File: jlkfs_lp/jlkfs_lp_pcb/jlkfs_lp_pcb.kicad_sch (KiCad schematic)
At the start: 40 parts, among them J0 USB_C_Receptacle_PowerOnly_6P, SW0 SWITCH, SW1 SWITCH, SW10 SWITCH, SW11 SWITCH, SW12 SWITCH, SW13 SWITCH, SW14 SWITCH, SW15 SWITCH, SW16 SWITCH, SW17 SWITCH, SW18 SWITCH, SW19 SWITCH, SW2 SWITCH, SW20 SWITCH, SW21 SWITCH, SW22 SWITCH, SW23 SWITCH, SW24 SWITCH, SW25 SWITCH, SW26 SWITCH, SW27 SWITCH, SW28 SWITCH, SW3 SWITCH, SW4 SWITCH, SW5 SWITCH, SW6 SWITCH, SW7 SWITCH, SW8 SWITCH, SW9 SWITCH, U0 RP2040

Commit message: Updates to jlkfs_lp.
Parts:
- removed H4, H5: MountingHole, MountingHole:MountingHole_3.5mm, symbol Mechanical:MountingHole
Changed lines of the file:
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@@
     (pin "11")
     (instances
-      (project "jlkfs_lower"
+      (project "jlkfs_lp_pcb"
         (path "/97127b28-60f4-45ff-835e-dccfbc833331"
           (reference "U0") (unit 1)
@@
     (pin "2")
     (instances
-      (project "jlkfs_lower"
+      (project "jlkfs_lp_pcb"
         (path "/97127b28-60f4-45ff-835e-dccfbc833331"
           (reference "SW13") (unit 1)
@@
     )
   )
-  (symbol (lib_id "Mechanical:MountingHole") (at 134.62 250.19 0) (unit 1)
-    (in_bom yes) (on_board yes) (dnp no) (fields_autoplaced)
-    (property "Reference" "H4" (at 137.16 248.92 0)
-      (effects (font (size 1.27 1.27)) (justify left))
-    )
-    (property "Value" "MountingHole" (at 137.16 251.46 0)
-      (effects (font (size 1.27 1.27)) (justify left))
-    )
-    (property "Footprint" "MountingHole:MountingHole_3.5mm" (at 134.62 250.19 0)
-      (effects (font (size 1.27 1.27)) hide)
-    )
-    (property "Datasheet" "~" (at 134.62 250.19 0)
-      (effects (font (size 1.27 1.27)) hide)
-    )
-    (instances
-      (project "jlkfs_lower"
-        (path "/97127b28-60f4-45ff-835e-dccfbc833331"
-          (reference "H4") (unit 1)
-        )
-      )
-    )
-  )
   (symbol (lib_id "symbols:SWITCH_WITH_DIODE") (at 198.12 77.47 0) (unit 1)
     (in_bom yes) (on_board yes) (dnp no) (fields_autoplaced)
@@
     (pin "2")
     (instances
-      (project "jlkfs_lower"
+      (project "jlkfs_lp_pcb"
         (path "/97127b28-60f4-45ff-835e-dccfbc833331"
           (reference "SW11") (unit 1)
@@
     (pin "2")
     (instances
-      (project "jlkfs_lower"
+      (project "jlkfs_lp_pcb"
         (path "/97127b28-60f4-45ff-835e-dccfbc833331"
           (reference "SW23") (unit 1)
@@
     (pin "2")
     (instances
-      (project "jlkfs_lower"
+      (project "jlkfs_lp_pcb"
         (path "/97127b28-60f4-45ff-835e-dccfbc833331"
           (reference "SW14") (unit 1)
@@
     (pin "2")
     (instances
-      (project "jlkfs_lower"
+      (project "jlkfs_lp_pcb"
         (path "/97127b28-60f4-45ff-835e-dccfbc833331"
           (reference "SW20") (unit 1)
@@
     (pin "2")
     (instances
-      (project "jlkfs_lower"
+      (project "jlkfs_lp_pcb"
         (path "/97127b28-60f4-45ff-835e-dccfbc833331"
           (reference "SW10") (unit 1)
@@
     (pin "2")
     (instances
-      (project "jlkfs_lower"
+      (project "jlkfs_lp_pcb"
         (path "/97127b28-60f4-45ff-835e-dccfbc833331"
           (reference "SW27") (unit 1)
@@
     (pin "2")
     (instances
-      (project "jlkfs_lower"
+      (project "jlkfs_lp_pcb"
         (path "/97127b28-60f4-45ff-835e-dccfbc833331"
           (reference "SW15") (unit 1)
@@
     (pin "2")
     (instances
-      (project "jlkfs_lower"
+      (project "jlkfs_lp_pcb"
         (path "/97127b28-60f4-45ff-835e-dccfbc833331"
           (reference "SW1") (unit 1)
@@
     (pin "2")
     (instances
-      (project "jlkfs_lower"
+      (project "jlkfs_lp_pcb"
         (path "/97127b28-60f4-45ff-835e-dccfbc833331"
           (reference "SW18") (unit 1)
@@
     (pin "2")
     (instances
-      (project "jlkfs_lower"
+      (project "jlkfs_lp_pcb"
         (path "/97127b28-60f4-45ff-835e-dccfbc833331"
           (reference "SW8") (unit 1)
@@
     (pin "2")
     (instances
-      (project "jlkfs_lower"
+      (project "jlkfs_lp_pcb"
         (path "/97127b28-60f4-45ff-835e-dccfbc833331"
           (reference "SW4") (unit 1)
@@
     (pin "2")
     (instances
-      (project "jlkfs_lower"
+      (project "jlkfs_lp_pcb"
         (path "/97127b28-60f4-45ff-835e-dccfbc833331"
           (reference "SW16") (unit 1)
@@
     (pin "2")
     (instances
-      (project "jlkfs_lower"
+      (project "jlkfs_lp_pcb"
         (path "/97127b28-60f4-45ff-835e-dccfbc833331"
           (reference "SW22") (unit 1)
@@
     (pin "2")
     (instances
-      (project "jlkfs_lower"
+      (project "jlkfs_lp_pcb"
         (path "/97127b28-60f4-45ff-835e-dccfbc833331"
           (reference "SW2") (unit 1)
@@
     (pin "2")
     (instances
-      (project "jlkfs_lower"
+      (project "jlkfs_lp_pcb"
         (path "/97127b28-60f4-45ff-835e-dccfbc833331"
           (reference "SW0") (unit 1)
@@
     )
     (instances
-      (project "jlkfs_lower"
+      (project "jlkfs_lp_pcb"
         (path "/97127b28-60f4-45ff-835e-dccfbc833331"
           (reference "H0") (unit 1)
@@
     (pin "2")
     (instances
-      (project "jlkfs_lower"
+      (project "jlkfs_lp_pcb"
         (path "/97127b28-60f4-45ff-835e-dccfbc833331"
           (reference "SW12") (unit 1)
@@
     )
     (instances
-      (project "jlkfs_lower"
+      (project "jlkfs_lp_pcb"
         (path "/97127b28-60f4-45ff-835e-dccfbc833331"
           (reference "H3") (unit 1)
@@
     (pin "1")
     (instances
-      (project "jlkfs_lower"
+      (project "jlkfs_lp_pcb"
         (path "/97127b28-60f4-45ff-835e-dccfbc833331"
           (reference "#PWR01") (unit 1)
@@
     (pin "2")
     (instances
-      (project "jlkfs_lower"
+      (project "jlkfs_lp_pcb"
         (path "/97127b28-60f4-45ff-835e-dccfbc833331"
           (reference "SW5") (unit 1)
@@
     (pin "2")
     (instances
-      (project "jlkfs_lower"
+      (project "jlkfs_lp_pcb"
         (path "/97127b28-60f4-45ff-835e-dccfbc833331"
           (reference "R1") (unit 1)
@@
     (pin "1")
     (instances
-      (project "jlkfs_lower"
+      (project "jlkfs_lp_pcb"
         (path "/97127b28-60f4-45ff-835e-dccfbc833331"
           (reference "#PWR02") (unit 1)
@@
     (pin "2")
     (instances
-      (project "jlkfs_lower"
+      (project "jlkfs_lp_pcb"
         (path "/97127b28-60f4-45ff-835e-dccfbc833331"
           (reference "SW7") (unit 1)
@@
     (pin "2")
     (instances
-      (project "jlkfs_lower"
+      (project "jlkfs_lp_pcb"
         (path "/97127b28-60f4-45ff-835e-dccfbc833331"
           (reference "SW9") (unit 1)
@@
     (pin "2")
     (instances
-      (project "jlkfs_lower"
+      (project "jlkfs_lp_pcb"
         (path "/97127b28-60f4-45ff-835e-dccfbc833331"
           (reference "SW3") (unit 1)
@@
     (pin "2")
     (instances
-      (project "jlkfs_lower"
+      (project "jlkfs_lp_pcb"
         (path "/97127b28-60f4-45ff-835e-dccfbc833331"
           (reference "SW26") (unit 1)
@@
     )
     (instances
-      (project "jlkfs_lower"
+      (project "jlkfs_lp_pcb"
         (path "/97127b28-60f4-45ff-835e-dccfbc833331"
           (reference "H2") (unit 1)
@@
     (pin "1")
     (instances
-      (project "jlkfs_lower"
+      (project "jlkfs_lp_pcb"
         (path "/97127b28-60f4-45ff-835e-dccfbc833331"
           (reference "#PWR00") (unit 1)
@@
     (pin "2")
     (instances
-      (project "jlkfs_lower"
+      (project "jlkfs_lp_pcb"
         (path "/97127b28-60f4-45ff-835e-dccfbc833331"
           (reference "SW24") (unit 1)
@@
     (pin "2")
     (instances
-      (project "jlkfs_lower"
+      (project "jlkfs_lp_pcb"
         (path "/97127b28-60f4-45ff-835e-dccfbc833331"
           (reference "SW28") (unit 1)
@@
     (pin "2")
     (instances
-      (project "jlkfs_lower"
+      (project "jlkfs_lp_pcb"
         (path "/97127b28-60f4-45ff-835e-dccfbc833331"
           (reference "R0") (unit 1)
@@
     (pin "2")
     (instances
-      (project "jlkfs_lower"
+      (project "jlkfs_lp_pcb"
         (path "/97127b28-60f4-45ff-835e-dccfbc833331"
           (reference "SW21") (unit 1)
@@
     )
     (instances
-      (project "jlkfs_lower"
+      (project "jlkfs_lp_pcb"
         (path "/97127b28-60f4-45ff-835e-dccfbc833331"
           (reference "H1") (unit 1)
@@
     (pin "2")
     (instances
-      (project "jlkfs_lower"
+      (project "jlkfs_lp_pcb"
         (path "/97127b28-60f4-45ff-835e-dccfbc833331"
           (reference "SW6") (unit 1)
@@
     (pin "2")
     (instances
-      (project "jlkfs_lower"
+      (project "jlkfs_lp_pcb"
         (path "/97127b28-60f4-45ff-835e-dccfbc833331"
           (reference "SW25") (unit 1)
@@
     (pin "A12")
     (instances
-      (project "jlkfs_lower"
+      (project "jlkfs_lp_pcb"
         (path "/97127b28-60f4-45ff-835e-dccfbc833331"
           (reference "J0") (unit 1)
@@
     (pin "2")
     (instances
-      (project "jlkfs_lower"
+      (project "jlkfs_lp_pcb"
         (path "/97127b28-60f4-45ff-835e-dccfbc833331"
           (reference "SW17") (unit 1)
@@
     (pin "2")
     (instances
-      (project "jlkfs_lower"
+      (project "jlkfs_lp_pcb"
         (path "/97127b28-60f4-45ff-835e-dccfbc833331"
           (reference "RST0") (unit 1)
@@
     )
   )
-  (symbol (lib_id "Mechanical:MountingHole") (at 138.43 250.19 0) (unit 1)
-    (in_bom yes) (on_board yes) (dnp no) (fields_autoplaced)
-    (property "Reference" "H5" (at 140.97 248.92 0)
-      (effects (font (size 1.27 1.27)) (justify left))
-    )
-    (property "Value" "MountingHole" (at 140.97 251.46 0)
-      (effects (font (size 1.27 1.27)) (justify left))
-    )
-    (property "Footprint" "MountingHole:MountingHole_3.5mm" (at 138.43 250.19 0)
-      (effects (font (size 1.27 1.27)) hide)
-    )
-    (property "Datasheet" "~" (at 138.43 250.19 0)
-      (effects (font (size 1.27 1.27)) hide)
-    )
-    (instances
-      (project "jlkfs_lower"
-        (path "/97127b28-60f4-45ff-835e-dccfbc833331"
-          (reference "H5") (unit 1)
-        )
-      )
-    )
-  )
   (symbol (lib_id "symbols:SWITCH_WITH_DIODE") (at 30.48 105.41 0) (unit 1)
     (in_bom yes) (on_board yes) (dnp no) (fields_autoplaced)
@@
     (pin "2")
     (instances
-      (project "jlkfs_lower"
+      (project "jlkfs_lp_pcb"
         (path "/97127b28-60f4-45ff-835e-dccfbc833331"
           (reference "SW19") (unit 1)

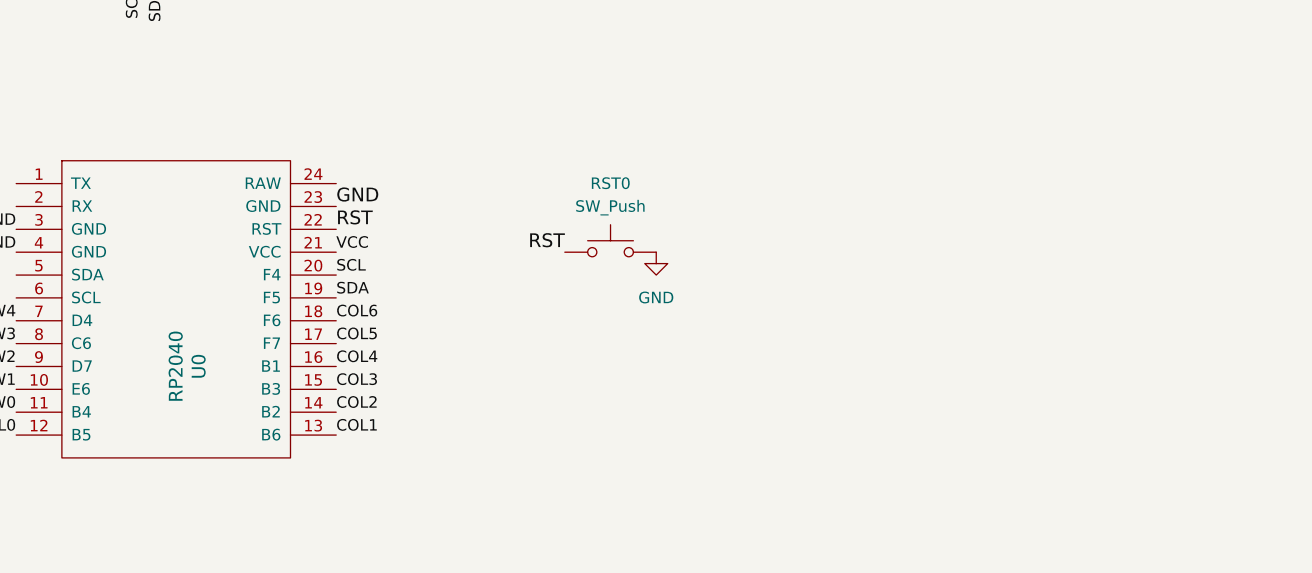
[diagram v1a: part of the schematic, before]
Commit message: Added a battery path for nice!nano to jlkfs.
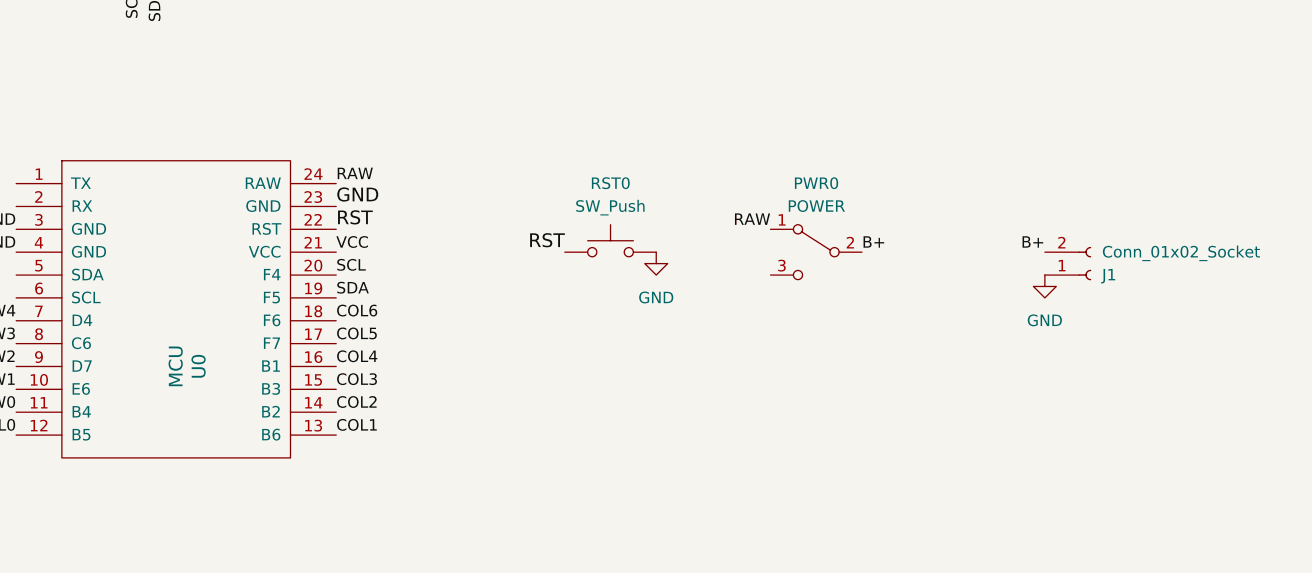
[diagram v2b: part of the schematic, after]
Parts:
- added J1: Conn_01x02_Socket, Connector_PinHeader_2.54mm:PinHeader_1x02_P2.54mm_Vertical, symbol Connector:Conn_01x02_Socket
- added PWR0: POWER, footprints:power_switch_1, symbol Switch:SW_SPDT
- U0: value RP2040 -> MCU
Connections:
- net GND: now also J1.1 (Pin_1)
- net RAW: now reaches U0.24 (RAW)
- net RAW: now also PWR0.1 (A)
- new net B+: J1.2 (Pin_2), PWR0.2 (B)
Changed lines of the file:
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@@
+    (effects (font (size 1.27 1.27)) (justify right bottom))
+  )
+  (label "B+" (at 215.9 198.12 180) (fields_autoplaced)
     (effects (font (size 1.27 1.27)) (justify right bottom))
   )
@@
     (effects (font (size 1.27 1.27)) (justify left bottom))
   )
+  (label "RAW" (at 185.42 195.58 180) (fields_autoplaced)
+    (effects (font (size 1.27 1.27)) (justify right bottom))
+  )
   (label "ROW2" (at 101.6 210.82 180) (fields_autoplaced)
     (effects (font (size 1.27 1.27)) (justify right bottom))
@@
     (effects (font (size 1.27 1.27)) (justify left bottom))
   )
+  (label "B+" (at 195.58 198.12 0) (fields_autoplaced)
+    (effects (font (size 1.27 1.27)) (justify left bottom))
+  )
   (label "ROW3" (at 101.6 208.28 180) (fields_autoplaced)
     (effects (font (size 1.27 1.27)) (justify right bottom))
@@
   )
   (label "COL5" (at 50.8 129.54 0) (fields_autoplaced)
+    (effects (font (size 1.27 1.27)) (justify left bottom))
+  )
+  (label "RAW" (at 137.16 190.5 0) (fields_autoplaced)
     (effects (font (size 1.27 1.27)) (justify left bottom))
   )
@@
       (effects (font (size 1.524 1.524)))
     )
-    (property "Value" "RP2040" (at 119.38 210.82 90)
+    (property "Value" "MCU" (at 119.38 210.82 90)
       (effects (font (size 1.524 1.524)))
     )
@@
     )
   )
+  (symbol (lib_id "Switch:SW_SPDT") (at 190.5 198.12 0) (mirror y) (unit 1)
+    (in_bom yes) (on_board yes) (dnp no)
+    (property "Reference" "PWR0" (at 190.5 190.5 0)
+      (effects (font (size 1.27 1.27)))
+    )
+    (property "Value" "POWER" (at 190.5 193.04 0)
+      (effects (font (size 1.27 1.27)))
+    )
+    (property "Footprint" "footprints:power_switch_1" (at 190.5 198.12 0)
+      (effects (font (size 1.27 1.27)) hide)
+    )
+    (property "Datasheet" "~" (at 190.5 198.12 0)
+      (effects (font (size 1.27 1.27)) hide)
+    )
+    (pin "1")
+    (pin "2")
+    (pin "3")
+    (instances
+      (project "jlkfs_lp_pcb"
+        (path "/97127b28-60f4-45ff-835e-dccfbc833331"
+          (reference "PWR0") (unit 1)
+        )
+      )
+    )
+  )
   (symbol (lib_id "symbols:SWITCH_WITH_DIODE") (at 198.12 77.47 0) (unit 1)
     (in_bom yes) (on_board yes) (dnp no) (fields_autoplaced)
@@
         (path "/97127b28-60f4-45ff-835e-dccfbc833331"
           (reference "SW9") (unit 1)
+        )
+      )
+    )
+  )
+  (symbol (lib_id "Connector:Conn_01x02_Socket") (at 220.98 200.66 0) (mirror x) (unit 1)
+    (in_bom yes) (on_board yes) (dnp no)
+    (property "Reference" "J1" (at 222.25 200.66 0)
+      (effects (font (size 1.27 1.27)) (justify left))
+    )
+    (property "Value" "Conn_01x02_Socket" (at 222.25 198.12 0)
+      (effects (font (size 1.27 1.27)) (justify left))
+    )
+    (property "Footprint" "Connector_PinHeader_2.54mm:PinHeader_1x02_P2.54mm_Vertical" (at 220.98 200.66 0)
+      (effects (font (size 1.27 1.27)) hide)
+    )
+    (property "Datasheet" "~" (at 220.98 200.66 0)
+      (effects (font (size 1.27 1.27)) hide)
+    )
+    (pin "1")
+    (pin "2")
+    (instances
+      (project "jlkfs_lp_pcb"
+        (path "/97127b28-60f4-45ff-835e-dccfbc833331"
+          (reference "J1") (unit 1)
         )
       )
@@
         )
       )
+    )
+  )
+  (symbol (lib_id "power:GND") (at 215.9 200.66 0) (unit 1)
+    (in_bom yes) (on_board yes) (dnp no) (fields_autoplaced)
+    (property "Reference" "#PWR03" (at 215.9 207.01 0)
+      (effects (font (size 1.27 1.27)) hide)
+    )
+    (property "Value" "GND" (at 215.9 205.74 0)
+      (effects (font (size 1.27 1.27)))
+    )
+    (property "Footprint" "" (at 215.9 200.66 0)
+      (effects (font (size 1.27 1.27)) hide)
+    )
+    (property "Datasheet" "" (at 215.9 200.66 0)
+      (effects (font (size 1.27 1.27)) hide)
+    )
+    (pin "1")
+    (instances
+      (project "jlkfs_lp_pcb"
+        (path "/97127b28-60f4-45ff-835e-dccfbc833331"
+          (reference "#PWR03") (unit 1)
+        )
+      )
